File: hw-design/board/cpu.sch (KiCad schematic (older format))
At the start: 22 parts, among them P1 CHAIN, P2 USB_OTG, P3 CONN_02X05, Q7 BC857, SW1 SW_PUSH, U4 LPC11U24FBD48/401, Y1 12MHz

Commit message: sch: setting footprints and updating BOM
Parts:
- P2: footprint (none) -> Connect:USB_Mini-B
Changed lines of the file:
@@
 F 0 "P2" H 3675 5975 50  0000 C CNN
 F 1 "USB_OTG" H 3350 6300 50  0000 C CNN
-F 2 "" V 3300 6000 60  0000 C CNN
+F 2 "Connect:USB_Mini-B" V 3300 6000 60  0000 C CNN
 F 3 "" V 3300 6000 60  0000 C CNN
 F 4 "10033526-N3212LF" H 0   0   50  0001 C CNN "MPN"

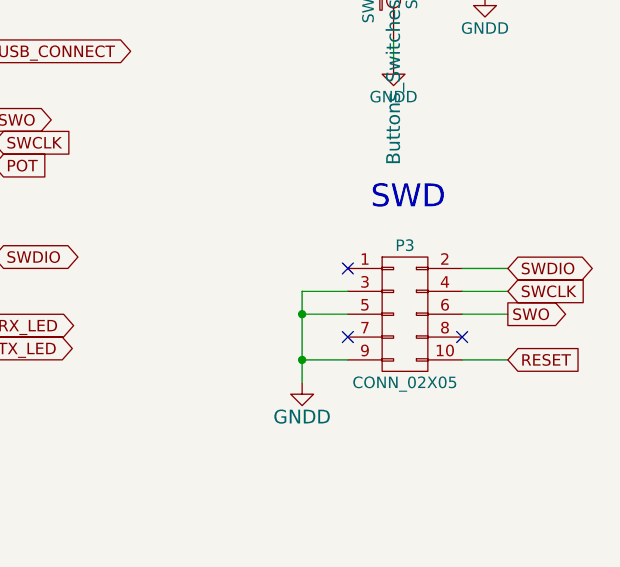
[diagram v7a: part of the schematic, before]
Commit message: fixing some footprints assignment
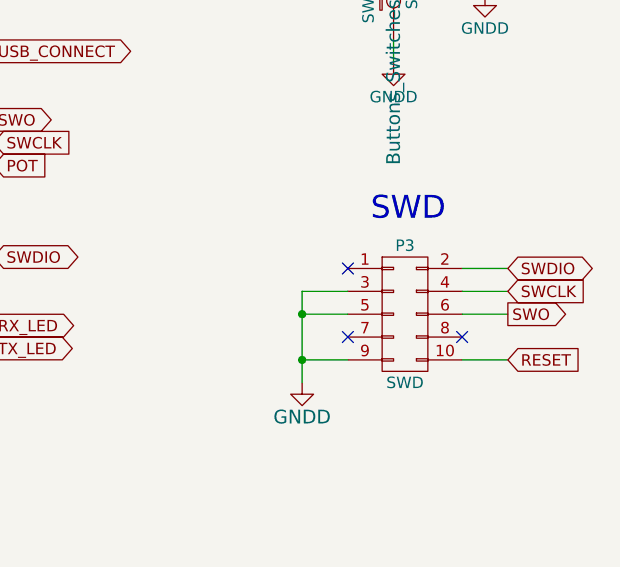
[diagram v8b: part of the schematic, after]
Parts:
- P3: value CONN_02X05 -> SWD
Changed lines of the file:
@@
 P 9650 3650
 F 0 "P3" H 9650 3950 50  0000 C CNN
-F 1 "CONN_02X05" H 9650 3350 50  0000 C CNN
+F 1 "SWD" H 9650 3350 50  0000 C CNN
 F 2 "Pin_Headers:Pin_Header_Straight_2x05_Pitch1.27mm" H 9650 2450 60  0001 C CNN
 F 3 "" H 9650 2450 60  0000 C CNN
@@
 Text GLabel 10100 3850 2    50   Input ~ 0
 RESET
-Text Notes 9500 3200 0    100  ~ 0
+Text Notes 9500 3250 0    100  ~ 0
 SWD
 Text GLabel 7850 2200 2    50   Input ~ 0
